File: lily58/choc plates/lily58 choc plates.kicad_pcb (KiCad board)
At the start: 2 copper layers, 137 x 100.1 mm, 34 parts, among them SW1 SW_PUSH, SW10 SW_PUSH, SW11 SW_PUSH, SW12 SW_PUSH, SW13 SW_PUSH, SW14 SW_PUSH, SW15 SW_PUSH, SW16 SW_PUSH, SW17 SW_PUSH, SW18 SW_PUSH, SW19 SW_PUSH, SW2 SW_PUSH, SW20 SW_PUSH, SW21 SW_PUSH, SW22 SW_PUSH, SW23 SW_PUSH, SW24 SW_PUSH, SW25 SW_PUSH, SW26 SW_PUSH, SW27 SW_PUSH, SW28 SW_PUSH, SW29 SW_PUSH, SW3 SW_PUSH, SW4 SW_PUSH, SW5 SW_PUSH, SW6 SW_PUSH, SW7 SW_PUSH, SW8 SW_PUSH, SW9 SW_PUSH

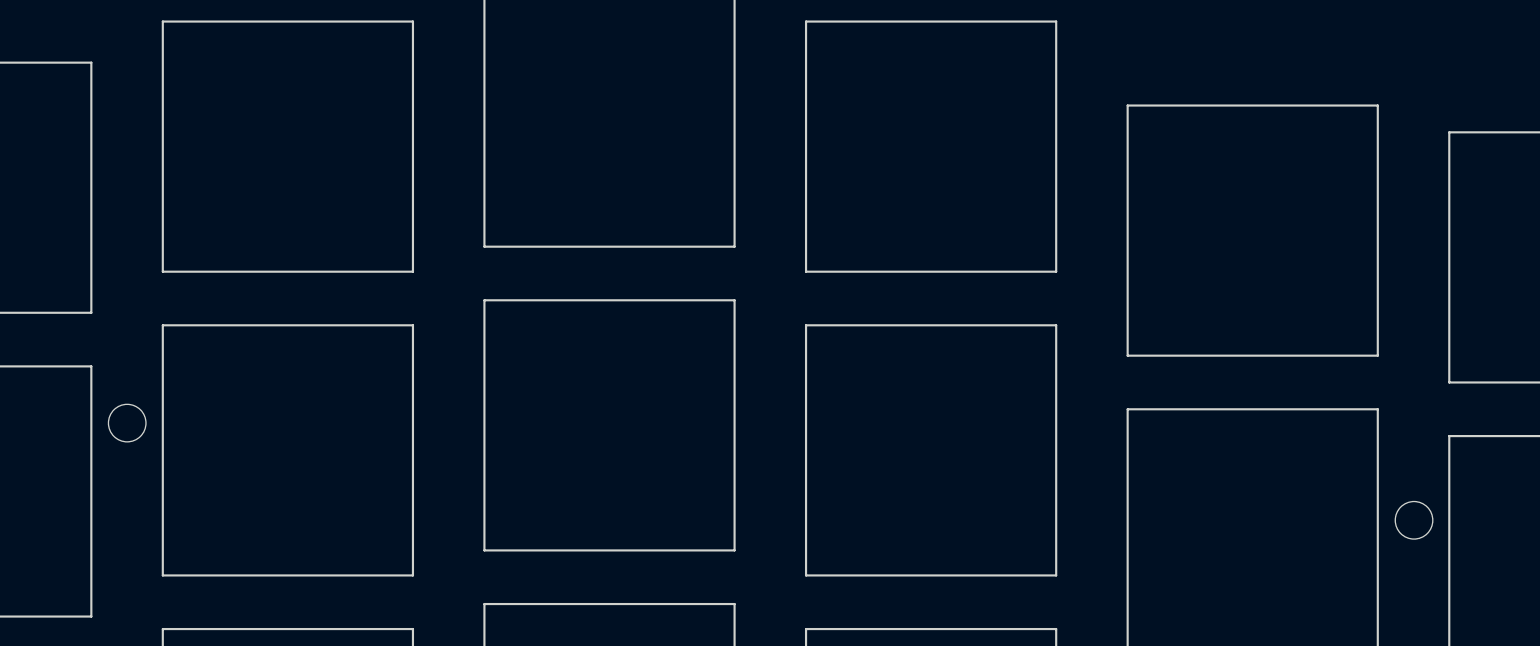
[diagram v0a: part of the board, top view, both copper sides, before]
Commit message: lily choc: move mounting holes
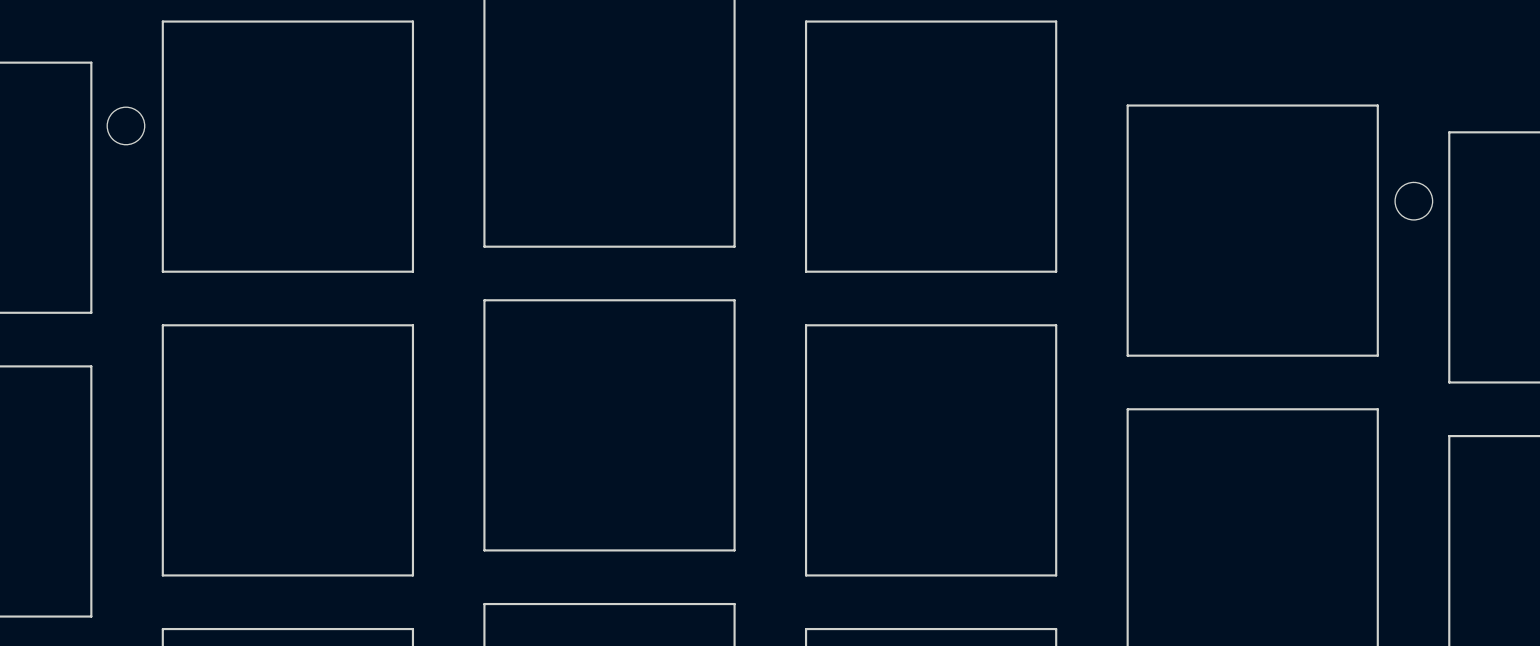
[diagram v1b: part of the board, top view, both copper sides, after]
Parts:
- moved TH4 17.9 mm to (141.2, 47.9)
- moved TH3 16.6 mm to (69.1, 43.7)
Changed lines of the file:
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@@
 	(footprint "holykeebs:M2_HOLE_NPH"
 		(layer "F.Cu")
-		(at 141.23 65.76)
+		(at 141.22 47.9)
 		(property "Reference" "TH4"
 			(at 0 -0.5 0)
@@
 			)
 		)
-		(property "Footprint" ""
+		(property "Footprint" "holykeebs:M2_HOLE_NPH"
 			(at 0 0 0)
 			(unlocked yes)
@@
 			)
 		)
-		(property "Footprint" ""
+		(property "Footprint" "holykeebs:M2_HOLE_NPH"
 			(at 0 0 0)
 			(unlocked yes)
@@
 			)
 		)
-		(property "Footprint" ""
+		(property "Footprint" "holykeebs:M2_HOLE_NPH"
 			(at 0 0 0)
 			(unlocked yes)
@@
 	(footprint "holykeebs:M2_HOLE_NPH"
 		(layer "F.Cu")
-		(at 69.21 60.32)
+		(at 69.14 43.69)
 		(property "Reference" "TH3"
 			(at 0 -0.5 0)
@@
 			)
 		)
-		(property "Footprint" ""
+		(property "Footprint" "holykeebs:M2_HOLE_NPH"
 			(at 0 0 0)
 			(unlocked yes)
@@
 			)
 		)
-		(property "Footprint" ""
+		(property "Footprint" "holykeebs:M2_HOLE_NPH"
 			(at 0 0 90)
 			(unlocked yes)
@@
 			)
 		)
-		(property "Footprint" ""
+		(property "Footprint" "kbd:SW_Hole"
 			(at 0 0 0)
 			(unlocked yes)
@@
 			)
 		)
-		(property "Footprint" ""
+		(property "Footprint" "kbd:SW_Hole"
 			(at 0 0 0)
 			(unlocked yes)
@@
 			)
 		)
-		(property "Footprint" ""
+		(property "Footprint" "kbd:SW_Hole"
 			(at 0 0 0)
 			(unlocked yes)
@@
 			)
 		)
-		(property "Footprint" ""
+		(property "Footprint" "kbd:SW_Hole"
 			(at 0 0 0)
 			(unlocked yes)
@@
 			)
 		)
-		(property "Footprint" ""
+		(property "Footprint" "kbd:SW_Hole"
 			(at 0 0 0)
 			(unlocked yes)
@@
 			)
 		)
-		(property "Footprint" ""
+		(property "Footprint" "kbd:SW_Hole"
 			(at 0 0 0)
 			(unlocked yes)
@@
 			)
 		)
-		(property "Footprint" ""
+		(property "Footprint" "kbd:SW_Hole"
 			(at 0 0 0)
 			(unlocked yes)
@@
 			)
 		)
-		(property "Footprint" ""
+		(property "Footprint" "kbd:SW_Hole"
 			(at 0 0 0)
 			(unlocked yes)
@@
 			)
 		)
-		(property "Footprint" ""
+		(property "Footprint" "kbd:SW_Hole"
 			(at 0 0 0)
 			(unlocked yes)
@@
 			)
 		)
-		(property "Footprint" ""
+		(property "Footprint" "kbd:SW_Hole"
 			(at 0 0 0)
 			(unlocked yes)
@@
 			)
 		)
-		(property "Footprint" ""
+		(property "Footprint" "kbd:SW_Hole"
 			(at 0 0 0)
 			(unlocked yes)
@@
 			)
 		)
-		(property "Footprint" ""
+		(property "Footprint" "kbd:SW_Hole"
 			(at 0 0 0)
 			(unlocked yes)
@@
 			)
 		)
-		(property "Footprint" ""
+		(property "Footprint" "kbd:SW_Hole"
 			(at 0 0 0)
 			(unlocked yes)
@@
 			)
 		)
-		(property "Footprint" ""
+		(property "Footprint" "kbd:SW_Hole"
 			(at 0 0 0)
 			(unlocked yes)
@@
 			)
 		)
-		(property "Footprint" ""
+		(property "Footprint" "kbd:SW_Hole"
 			(at 0 0 -60)
 			(unlocked yes)
@@
 			)
 		)
-		(property "Footprint" ""
+		(property "Footprint" "kbd:SW_Hole"
 			(at 0 0 0)
 			(unlocked yes)
@@
 			)
 		)
-		(property "Footprint" ""
+		(property "Footprint" "kbd:SW_Hole"
 			(at 0 0 0)
 			(unlocked yes)
@@
 			)
 		)
-		(property "Footprint" ""
+		(property "Footprint" "kbd:SW_Hole"
 			(at 0 0 0)
 			(unlocked yes)
@@
 			)
 		)
-		(property "Footprint" ""
+		(property "Footprint" "kbd:SW_Hole"
 			(at 0 0 0)
 			(unlocked yes)
@@
 			)
 		)
-		(property "Footprint" ""
+		(property "Footprint" "kbd:SW_Hole"
 			(at 0 0 0)
 			(unlocked yes)
@@
 			)
 		)
-		(property "Footprint" ""
+		(property "Footprint" "kbd:SW_Hole"
 			(at 0 0 0)
 			(unlocked yes)
@@
 			)
 		)
-		(property "Footprint" ""
+		(property "Footprint" "kbd:SW_Hole"
 			(at 0 0 0)
 			(unlocked yes)
@@
 			)
 		)
-		(property "Footprint" ""
+		(property "Footprint" "kbd:SW_Hole"
 			(at 0 0 0)
 			(unlocked yes)
@@
 			)
 		)
-		(property "Footprint" ""
+		(property "Footprint" "kbd:SW_Hole"
 			(at 0 0 0)
 			(unlocked yes)
@@
 			)
 		)
-		(property "Footprint" ""
+		(property "Footprint" "kbd:SW_Hole"
 			(at 0 0 0)
 			(unlocked yes)
@@
 			)
 		)
-		(property "Footprint" ""
+		(property "Footprint" "kbd:SW_Hole"
 			(at 0 0 0)
 			(unlocked yes)
@@
 			)
 		)
-		(property "Footprint" ""
+		(property "Footprint" "kbd:SW_Hole"
 			(at 0 0 0)
 			(unlocked yes)
@@
 			)
 		)
-		(property "Footprint" ""
+		(property "Footprint" "kbd:SW_Hole"
 			(at 0 0 0)
 			(unlocked yes)
@@
 			)
 		)
-		(property "Footprint" ""
+		(property "Footprint" "kbd:SW_Hole"
 			(at 0 0 0)
 			(unlocked yes)
